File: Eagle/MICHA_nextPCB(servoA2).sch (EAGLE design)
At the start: 57 parts, among them IC1 LM4041A12LP, K1 PIN20X2, T1 BSS84, U1 ARDUINO_MKR_ZERO, U2 MIKROE_CLICK, X1 SS-7188S-A-NF_V2, X2 SS-7188S-A-NF_V2, X3 SS-7188S-A-NF_V2, X4 SS-7188S-A-NF_V2, X5 SS-7188S-A-NF_V2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

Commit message: Update for next PCB version
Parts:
- removed TVS3: 5Vdc/12pF, EMCComponents (rev19b):WE-TVS_SOT23-3L_824022
- removed Z3, Z4: 3,3V, Zener_SMA:ZENER_SMA
- added O1: HMHA281R2, HMHA281R2:HMHA281R2
- added R18: 390, resistor:R-EU_R1206
- added R19: 2k, resistor:R-EU_R1206
- R1, R2: value 180 -> 100
- R12, R8, R9: device rcl:R-EU_R1210 -> rcl:R-EU_R1206
- R6: value 15-1/4W -> 680
- R7: value 15-1/4W -> 1k
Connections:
- removed net N$1: R17.2, T1.S, U1.3V3
- removed net N$14: C13.1, R6.2, TVS3.I/O2, U1.A2, Z3.C
- removed net PUMP_SERVO: R6.1, X4.6
- new net N$7: O1.A, R18.2
- new net N$9: C13.1, O1.COL, R6.1, U1.A2
- new net PUMP_SERVO_A+: R18.1, X4.6
- new net PUMP_SERVO_A-: O1.C, X4.3
- new net VDD: R17.2, R6.2, T1.S, U1.3V3
- net D19: now also R19.2; no longer TVS3.I/O1, Z4.C
- net GND: now also O1.EMIT, R19.1; no longer TVS3.GND, X4.3, Z3.A, Z4.A
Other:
- moved on the sheet: C10, C11, C13, C2, C8, C9, R13, R14, R15, R16, R6, R7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

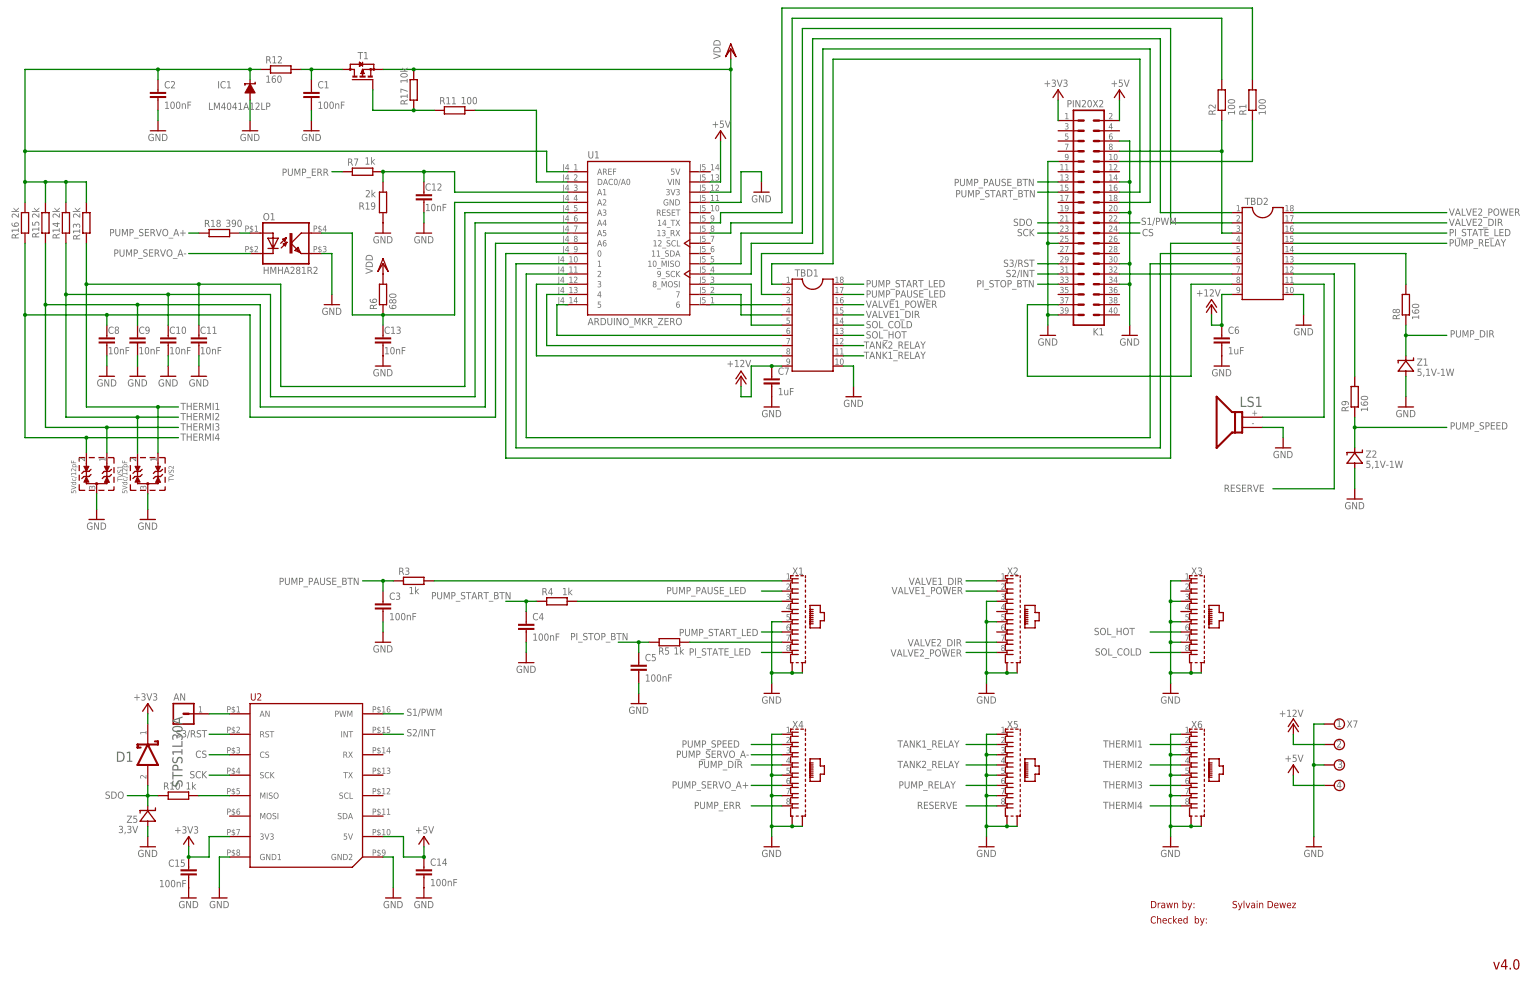
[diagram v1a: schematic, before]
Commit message: MICHA_nextPCB updated
- analog switch added
- zener and tvs for protection added
- schottky diode deleted
- error signal go through a bridge divider instead of a zener
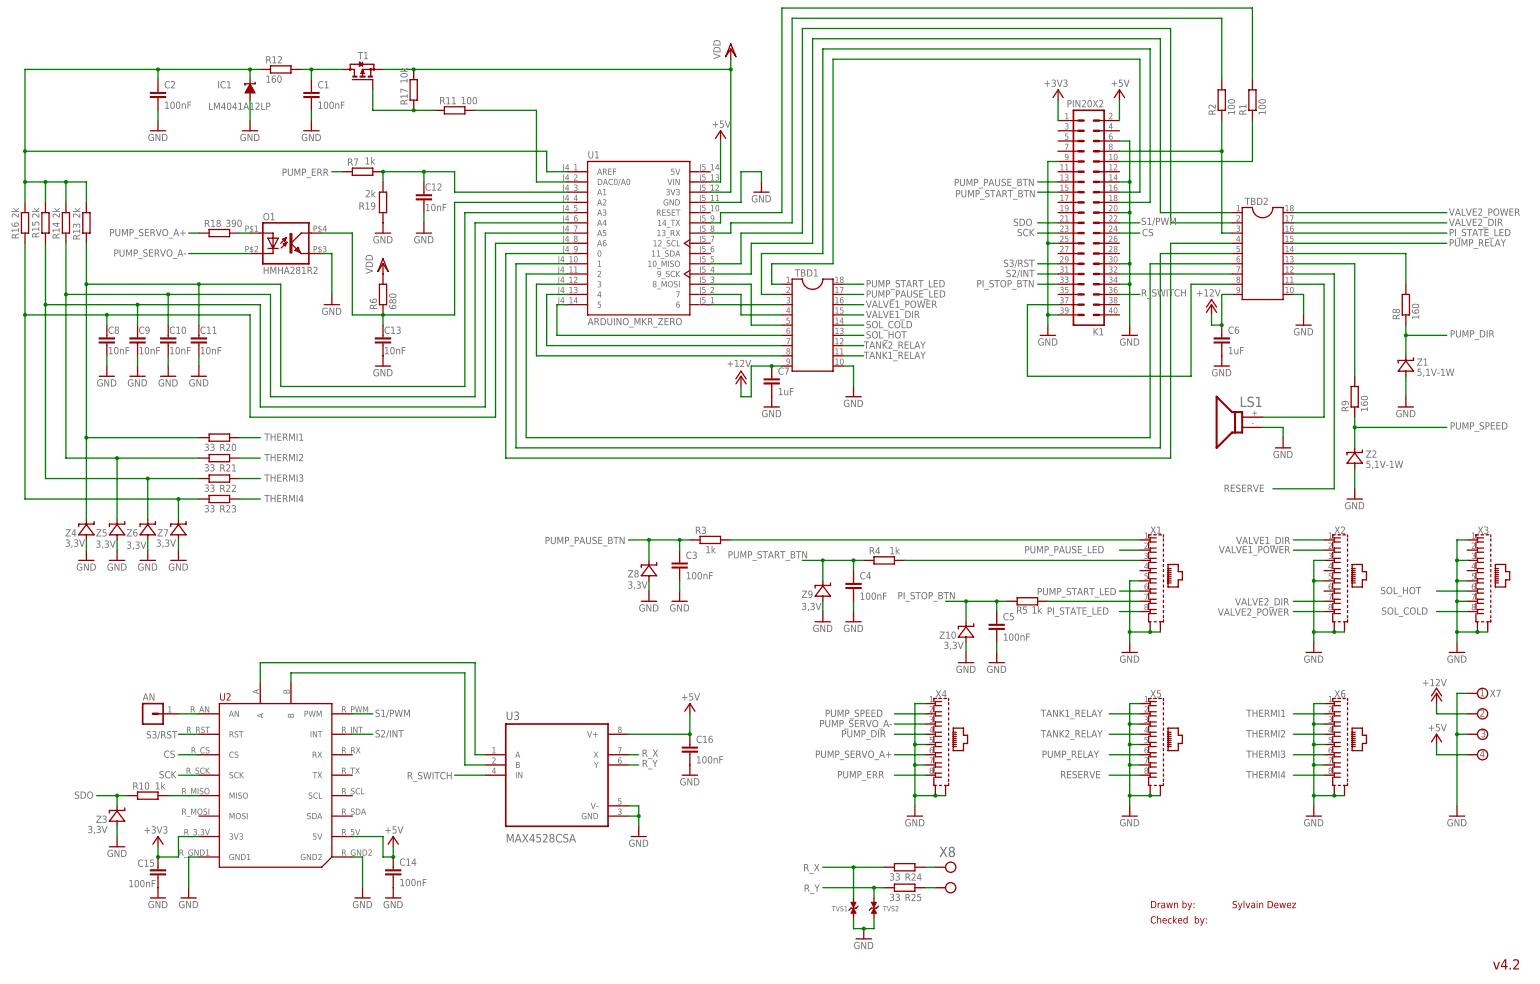
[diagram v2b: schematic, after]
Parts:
- removed D1: STMICROELECTRONICS_STPS1L30ASTMICROELECTRONICS_STPS1L30A_0_0, Diode_STPS1L30A:STMICROELECTRONICS_STPS1L30ASTMICROELECTRONICS_STPS1L30A_0_0
- added C16: 100nF, rcl:C-EUC1206
- added R20, R21, R22, R23, R24, R25: 33, resistor:R-EU_R1206
- added U3: MAX4528CSA, MAX4528CSA:MAX4528CSA
- added X8: MPT_0,5/_2-2,54_1725656_2, MPT_0_5__2-2_54_1725656:MPT_0,5/_2-2,54_1725656_2
- added Z10, Z3, Z4, Z6, Z7, Z8, Z9: 3,3V, Zener_SMA:ZENER_SMA
- TVS1, TVS2: value 5Vdc/12pF -> TVS_SOD123; device EMCComponents (rev19b):WE-TVS_SOT23-3L_824022 -> TV02W6V0B-G_SOD123:TVS_SOD123
- U2: value MIKROE_CLICK -> MIKROE_CLICK_UPGRADE; device mikrobus_lib:MIKROE_CLICK -> mikrobus_lib:MIKROE_CLICK_UPGRADE
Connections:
- net AN renamed N$16
- net MISO renamed N$15
- new net N$1: U2.B, U3.B
- new net N$10: U2.A, U3.A
- new net N$11: C11.1, R13.2, R20.1, U1.A3, Z4.C
- new net N$12: C10.1, R14.2, R21.1, U1.A4, Z5.C
- new net N$13: C9.1, R15.2, R22.1, U1.A5, Z6.C
- new net N$14: C8.1, R16.2, R23.1, U1.A6, Z7.C
- new net N$17: R24.2, X8.KL1
- new net N$18: R25.2, X8.KL
- new net R_SWITCH: K1.36, U3.IN
- new net R_X: R24.1, TVS1.C, U3.X
- new net R_Y: R25.1, TVS2.C, U3.Y
- net +3V3: no longer D1.CATHODE
- net +5V: now also C16.1, U3.V+
- net GND: now also C16.2, TVS1.C1, TVS2.C1, U3.GND, U3.V-, Z10.A, Z3.A, Z4.A, Z6.A, Z7.A, Z8.A, Z9.A; no longer TVS1.GND, TVS2.GND
- net PI_STOP_BTN: now also Z10.C
- net PUMP_PAUSE_BTN: now also Z8.C
- net PUMP_START_BTN: now also Z9.C
- net SDO: now also Z3.C; no longer D1.ANODE, Z5.C
- net THERMI1: now also R20.2; no longer C11.1, R13.2, TVS2.I/O1, U1.A3
- net THERMI2: now also R21.2; no longer C10.1, R14.2, TVS2.I/O2, U1.A4
- net THERMI3: now also R22.2; no longer C9.1, R15.2, TVS1.I/O1, U1.A5
- net THERMI4: now also R23.2; no longer C8.1, R16.2, TVS1.I/O2, U1.A6
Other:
- note added: "v4.2"
- note removed: "v4.0"
- moved on the sheet: AN, C14, C15, C3, C4, C5, R10, R3, R4, R5, X1, X2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

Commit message: MICHA_nextPCB eagle files updated
3.3V source of Mikro deleted
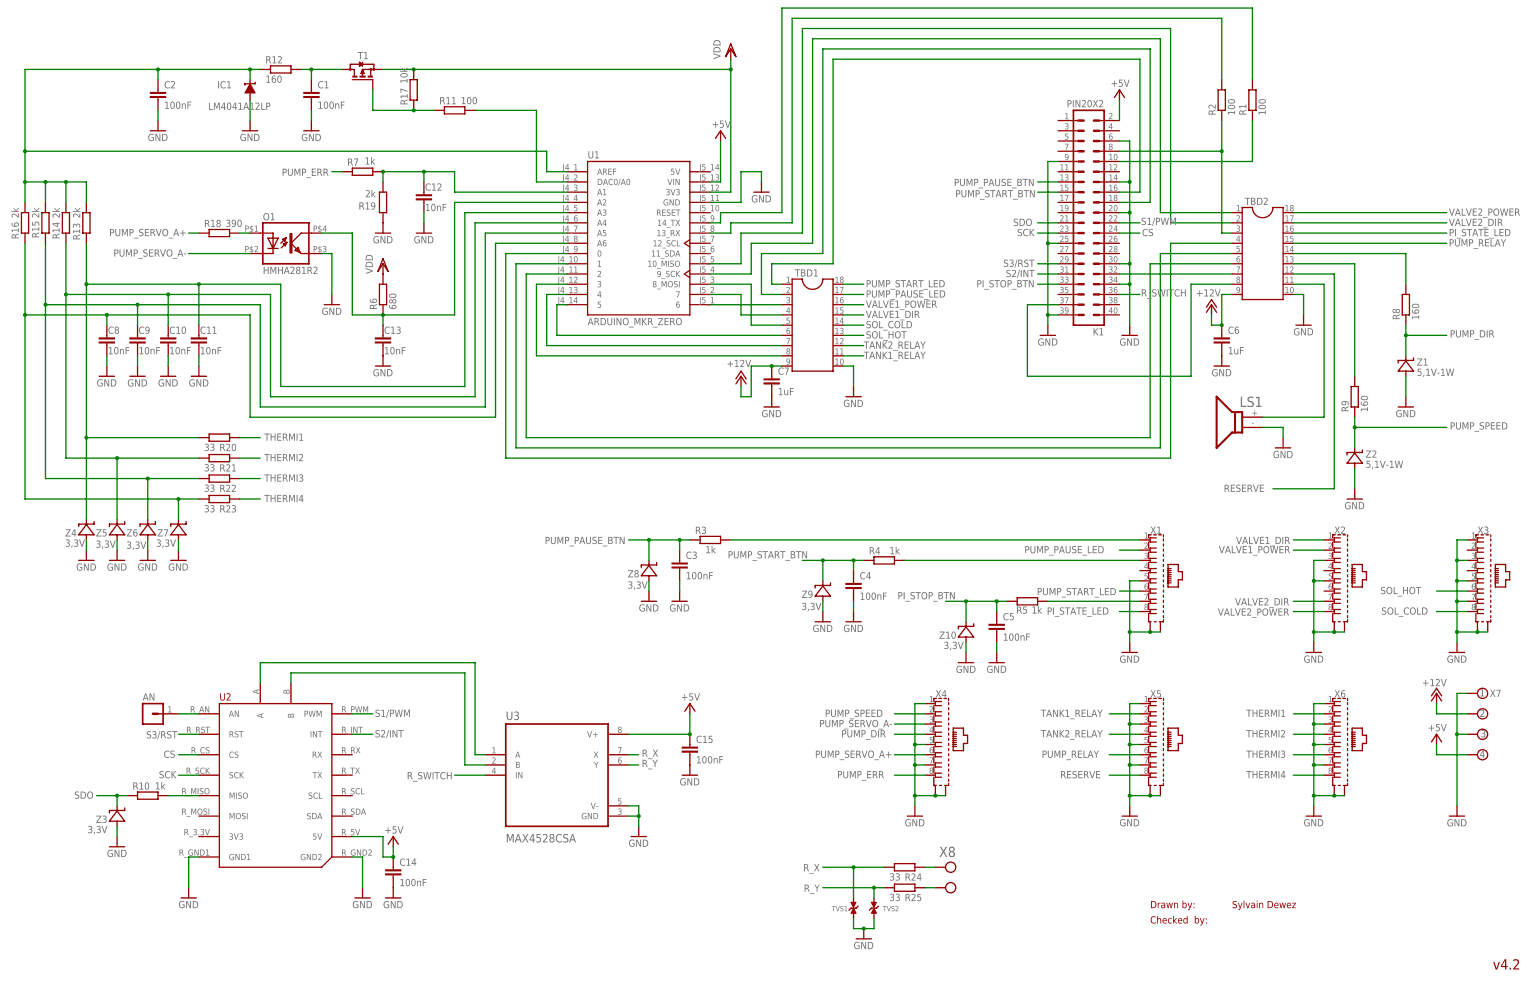
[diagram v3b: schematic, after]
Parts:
- removed C16: 100nF, rcl:C-EUC1206
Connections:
- removed net +3V3: C15.1, K1.1, U2.3V3
- net +5V: now also C15.1; no longer C16.1
- net GND: no longer C16.2
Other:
- moved on the sheet: C15
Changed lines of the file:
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@@
 <part name="GND35" library="supply1" deviceset="GND" device=""/>
 <part name="GND36" library="supply1" deviceset="GND" device=""/>
-<part name="+3V1" library="supply1" library_urn="urn:adsk.eagle:library:371" deviceset="+3V3" device=""/>
-<part name="+3V2" library="supply1" library_urn="urn:adsk.eagle:library:371" deviceset="+3V3" device=""/>
 <part name="P+8" library="supply1" deviceset="+5V" device=""/>
 <part name="C14" library="rcl" library_urn="urn:adsk.eagle:library:334" deviceset="C-EU" device="C1206" package3d_urn="urn:adsk.eagle:package:23618/2" value="100nF"/>
 <part name="GND37" library="supply1" deviceset="GND" device=""/>
-<part name="C15" library="rcl" library_urn="urn:adsk.eagle:library:334" deviceset="C-EU" device="C1206" package3d_urn="urn:adsk.eagle:package:23618/2" value="100nF"/>
-<part name="GND38" library="supply1" deviceset="GND" device=""/>
 <part name="U2" library="mikrobus_lib" deviceset="MIKROE_CLICK_UPGRADE" device=""/>
 <part name="R10" library="resistor" deviceset="R-EU_" device="R1206" value="1k"/>
@@
 <part name="Z10" library="Zener_SMA" deviceset="ZENER_SMA" device="" value="3,3V"/>
 <part name="GND45" library="supply1" deviceset="GND" device=""/>
-<part name="C16" library="rcl" library_urn="urn:adsk.eagle:library:334" deviceset="C-EU" device="C1206" package3d_urn="urn:adsk.eagle:package:23618/2" value="100nF"/>
+<part name="C15" library="rcl" library_urn="urn:adsk.eagle:library:334" deviceset="C-EU" device="C1206" package3d_urn="urn:adsk.eagle:package:23618/2" value="100nF"/>
 <part name="GND46" library="supply1" deviceset="GND" device=""/>
 <part name="R24" library="resistor" deviceset="R-EU_" device="R1206" value="33"/>
@@
 <attribute name="VALUE" x="48.26" y="20.32" size="1.778" layer="96"/>
 </instance>
-<instance part="+3V1" gate="G$1" x="266.7" y="223.52" smashed="yes">
-<attribute name="VALUE" x="269.24" y="226.06" size="1.778" layer="96" rot="R180"/>
-</instance>
-<instance part="+3V2" gate="G$1" x="43.18" y="38.1" smashed="yes">
-<attribute name="VALUE" x="45.72" y="40.64" size="1.778" layer="96" rot="R180"/>
-</instance>
 <instance part="P+8" gate="1" x="101.6" y="38.1" smashed="yes">
 <attribute name="VALUE" x="104.14" y="40.64" size="1.778" layer="96" rot="R180"/>
@@
 <attribute name="VALUE" x="99.06" y="20.32" size="1.778" layer="96"/>
 </instance>
-<instance part="C15" gate="G$1" x="43.18" y="30.48" smashed="yes">
-<attribute name="NAME" x="38.1" y="30.607" size="1.778" layer="95"/>
-<attribute name="VALUE" x="35.814" y="25.527" size="1.778" layer="96"/>
-</instance>
-<instance part="GND38" gate="1" x="43.18" y="22.86" smashed="yes">
-<attribute name="VALUE" x="40.64" y="20.32" size="1.778" layer="96"/>
-</instance>
 <instance part="U2" gate="G$1" x="73.66" y="53.34" smashed="yes">
 <attribute name="NAME" x="58.42" y="71.882" size="1.778" layer="94"/>
@@
 <attribute name="VALUE" x="241.3" y="78.74" size="1.778" layer="96"/>
 </instance>
-<instance part="C16" gate="G$1" x="175.26" y="60.96" smashed="yes">
+<instance part="C15" gate="G$1" x="175.26" y="60.96" smashed="yes">
 <attribute name="NAME" x="176.784" y="61.341" size="1.778" layer="95"/>
 <attribute name="VALUE" x="176.784" y="56.261" size="1.778" layer="96"/>
@@
 </segment>
 <segment>
-<pinref part="GND38" gate="1" pin="GND"/>
-<pinref part="C15" gate="G$1" pin="2"/>
-</segment>
-<segment>
 <pinref part="U2" gate="G$1" pin="GND2"/>
 <wire x1="91.44" y1="33.02" x2="93.98" y2="33.02" width="0.1524" layer="91"/>
@@
 <segment>
 <pinref part="GND46" gate="1" pin="GND"/>
-<pinref part="C16" gate="G$1" pin="2"/>
+<pinref part="C15" gate="G$1" pin="2"/>
 </segment>
 </net>
@@
 <wire x1="160.02" y1="63.5" x2="175.26" y2="63.5" width="0.1524" layer="91"/>
 <wire x1="175.26" y1="63.5" x2="175.26" y2="68.58" width="0.1524" layer="91"/>
-<pinref part="C16" gate="G$1" pin="1"/>
+<pinref part="C15" gate="G$1" pin="1"/>
 <junction x="175.26" y="63.5"/>
 </segment>
@@
 </segment>
 </net>
-<net name="+3V3" class="0">
-<segment>
-<pinref part="K1" gate="G$1" pin="1"/>
-<pinref part="+3V1" gate="G$1" pin="+3V3"/>
-<wire x1="266.7" y1="215.9" x2="266.7" y2="220.98" width="0.1524" layer="91"/>
-</segment>
-<segment>
-<pinref part="+3V2" gate="G$1" pin="+3V3"/>
-<wire x1="43.18" y1="33.02" x2="43.18" y2="35.56" width="0.1524" layer="91"/>
-<pinref part="C15" gate="G$1" pin="1"/>
-<pinref part="U2" gate="G$1" pin="3V3"/>
-<wire x1="53.34" y1="38.1" x2="48.26" y2="38.1" width="0.1524" layer="91"/>
-<wire x1="48.26" y1="38.1" x2="48.26" y2="33.02" width="0.1524" layer="91"/>
-<wire x1="48.26" y1="33.02" x2="43.18" y2="33.02" width="0.1524" layer="91"/>
-<junction x="43.18" y="33.02"/>
-</segment>
-</net>
